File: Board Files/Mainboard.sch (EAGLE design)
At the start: 109 parts, among them J1 I2C Display

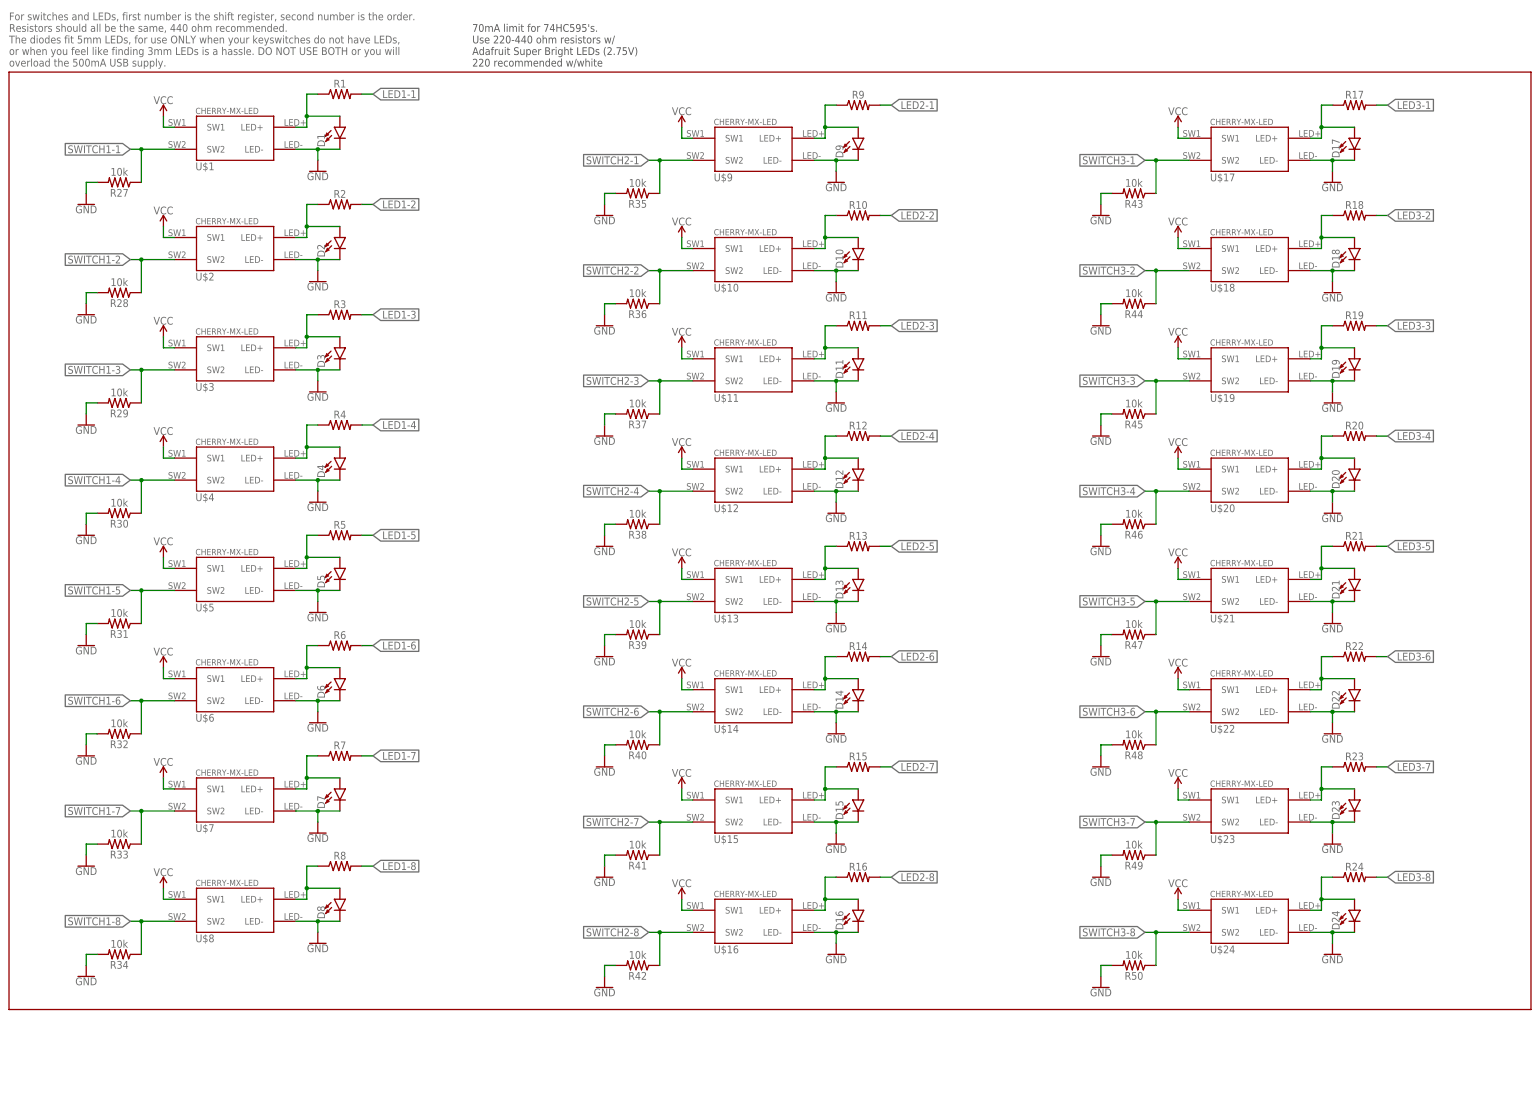
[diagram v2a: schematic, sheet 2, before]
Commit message: Completed First Schematic Draft
-Switched to Sparkfun Cherry parts
-Added illuminated rotary encoder
-Connected all microcontroller pins
-Finished shift register pins
-Added octave shift buttons
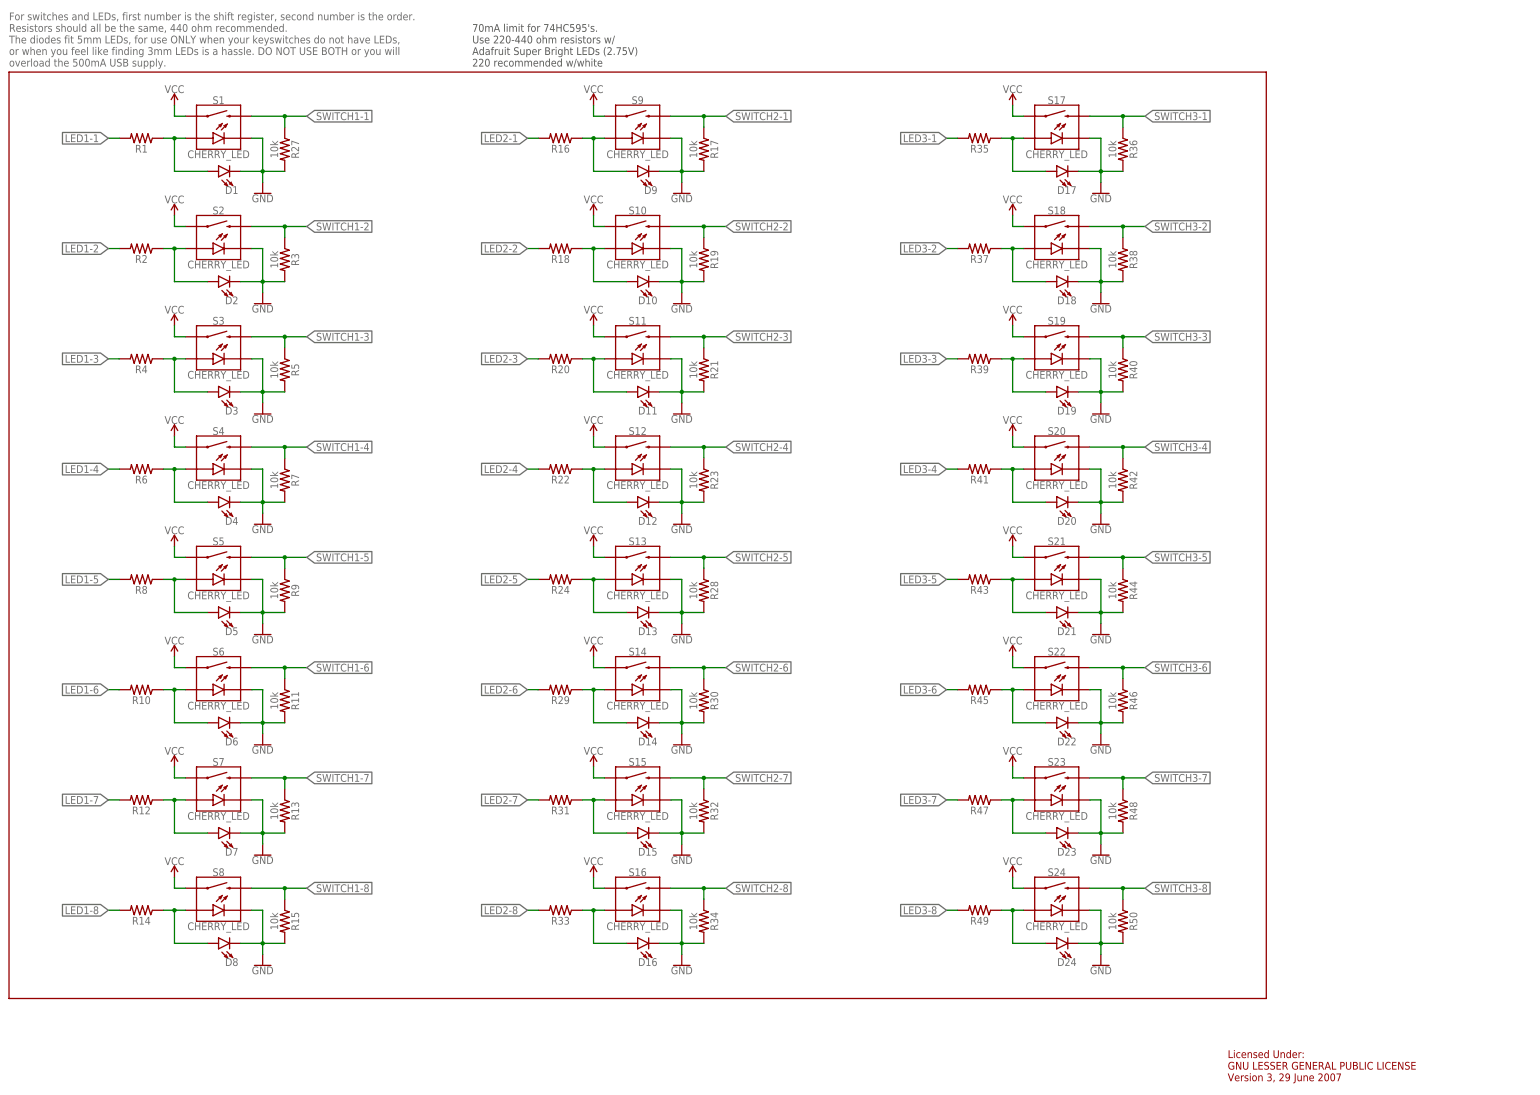
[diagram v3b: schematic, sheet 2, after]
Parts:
- removed U$1, U$10, U$11, U$12, U$13, U$14, U$15, U$16, U$17, U$18, U$19, U$2, U$20, U$21, U$22, U$23, U$24, U$3, U$4, U$5, U$6, U$7, U$8, U$9: CHERRY-MX-LED, cherrymx:CHERRY-MX-LED
- added R51, R52, R55: 10k, SparkFun-Resistors:10KOHM-HORIZ-1/4W-1%
- added S10, S11, S12, S13, S14, S15, S16, S17, S18, S19, S2, S20, S21, S22, S23, S24, S26, S27, S3, S4, S5, S6, S7, S8, S9: CHERRY_LED, SparkFun-Switches:MOMENTARY-SWITCH-SPST-LED-PTH-CHERRY
- added S25: 6MM_SPST_SMD_SWITCH, SparkFun-Switches:MOMENTARY-SWITCH-SPST-SMD-6.0X3.5MM
- added S28: ENCODER-2LED, SparkFun-Switches:ENCODER-2LED
- R11, R13, R15, R17, R19, R21, R23, R3, R5, R7, R9: value (none) -> 10k; device SparkFun-Resistors:RESISTORAXIAL-0.3 -> SparkFun-Resistors:10KOHM-HORIZ-1/4W-1%
- R29, R31, R33, R35, R37, R39, R41, R43, R45, R47, R49: value 10k -> (none); device SparkFun-Resistors:10KOHM-HORIZ-1/4W-1% -> SparkFun-Resistors:RESISTORAXIAL-0.3
- S1: value MOMENTARY-SWITCH-6MM-SMD -> CHERRY_LED; device SparkFun-Switches:MOMENTARY-SWITCH-SPST-SMD-6.0X3.5MM -> SparkFun-Switches:MOMENTARY-SWITCH-SPST-LED-PTH-CHERRY
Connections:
- removed net LED_CLOCK: B1.*5, LED_REG_1.SCK, LED_REG_2.SCK, LED_REG_3.SCK
- removed net N$28: B1.7
- removed net N$29: B1.8
- new net ENCODER_ANALOG: B1.A0, S28.B
- new net ENCODER_DIGITAL: B1.13(SCK), S28.A
- new net ENCODER_GREEN: B1.A2, S28.+G
- new net ENCODER_RED: B1.A1, S28.+R
- new net ENCODER_SWITCH: B1.A3, R55.1, S28.SW
- new net LED_OUTPUT_EN: B1.*6
- new net OCTAVE_DOWN: B1.11(MOSI), R52.2, S27.2
- new net OCTAVE_UP: B1.12(MISO), R51.2, S26.2
- new net REGISTER_CLOCK: B1.*9, KEY_REG_1A.CLK, LED_REG_1.SCK, LED_REG_2.SCK, LED_REG_3.SCK
- net GND: now also B1.GND@2, R11.2, R13.2, R15.2, R17.2, R19.2, R21.2, R23.2, R3.2, R5.2, R51.1, R52.1, R7.2, R9.2, S1.C, S10.C, S11.C, S12.C, S13.C, S14.C, S15.C, S16.C, S17.C, S18.C, S19.C, S2.C, S20.C, S21.C, S22.C, S23.C, S24.C, S25.2, S28.-, S28.C, S3.C, S4.C, S5.C, S6.C, S7.C, S8.C, S9.C; no longer R29.2, R31.2, R33.2, R35.2, R37.2, R39.2, R41.2, R43.2, R45.2, R47.2, R49.2, S1.2, U$1.LED-, U$10.LED-, U$11.LED-, U$12.LED-, U$13.LED-, U$14.LED-, U$15.LED-, U$16.LED-, U$17.LED-, U$18.LED-, U$19.LED-, U$2.LED-, U$20.LED-, U$21.LED-, U$22.LED-, U$23.LED-, U$24.LED-, U$3.LED-, U$4.LED-, U$5.LED-, U$6.LED-, U$7.LED-, U$8.LED-, U$9.LED-
- net KEY_CLOCK: no longer KEY_REG_1A.CLK
- net KEY_DATA: now also B1.7
- net KEY_LATCH: now also B1.8
- net LED1-3: now also R4.2; no longer R3.2
- net LED1-4: now also R6.2; no longer R4.2
- net LED1-5: now also R8.2; no longer R5.2
- net LED1-6: now also R10.2; no longer R6.2
- net LED1-7: now also R12.2; no longer R7.2
- net LED1-8: now also R14.2; no longer R8.2
- net LED2-1: now also R16.2; no longer R9.2
- net LED2-2: now also R18.2; no longer R10.2
- net LED2-3: now also R20.2; no longer R11.2
- net LED2-4: now also R22.2; no longer R12.2
- net LED2-5: now also R24.2; no longer R13.2
- net LED2-6: now also R29.2; no longer R14.2
- net LED2-7: now also R31.2; no longer R15.2
- net LED2-8: now also R33.2; no longer R16.2
- net LED3-1: now also R35.2; no longer R17.2
- net LED3-2: now also R37.2; no longer R18.2
- net LED3-3: now also R39.2; no longer R19.2
- net LED3-4: now also R41.2; no longer R20.2
- net LED3-5: now also R43.2; no longer R21.2
- net LED3-6: now also R45.2; no longer R22.2
- net LED3-7: now also R47.2; no longer R23.2
- net LED3-8: now also R49.2; no longer R24.2
- net LED_LATCH: now also B1.*5; no longer B1.*6
- net N$1: now also S1.A; no longer U$1.LED+
- net N$10: now also R18.1, S10.A; no longer R10.1, U$10.LED+
- net N$11: now also R20.1, S11.A; no longer R11.1, U$11.LED+
- net N$12: now also R22.1, S12.A; no longer R12.1, U$12.LED+
- net N$13: now also R24.1, S13.A; no longer R13.1, U$13.LED+
- net N$14: now also R29.1, S14.A; no longer R14.1, U$14.LED+
- net N$15: now also R31.1, S15.A; no longer R15.1, U$15.LED+
- net N$16: now also R33.1, S16.A; no longer R16.1, U$16.LED+
- net N$17: now also R35.1, S17.A; no longer R17.1, U$17.LED+
- net N$18: now also R37.1, S18.A; no longer R18.1, U$18.LED+
- net N$19: now also R39.1, S19.A; no longer R19.1, U$19.LED+
- net N$2: now also S2.A; no longer U$2.LED+
- net N$20: now also R41.1, S20.A; no longer R20.1, U$20.LED+
- net N$21: now also R43.1, S21.A; no longer R21.1, U$21.LED+
- net N$22: now also R45.1, S22.A; no longer R22.1, U$22.LED+
- net N$23: now also R47.1, S23.A; no longer R23.1, U$23.LED+
- net N$24: now also R49.1, S24.A; no longer R24.1, U$24.LED+
- net N$3: now also R4.1, S3.A; no longer R3.1, U$3.LED+
- net N$4: now also R6.1, S4.A; no longer R4.1, U$4.LED+
- net N$5: now also R8.1, S5.A; no longer R5.1, U$5.LED+
- net N$6: now also R10.1, S6.A; no longer R6.1, U$6.LED+
- net N$7: now also R12.1, S7.A; no longer R7.1, U$7.LED+
- net N$8: now also R14.1, S8.A; no longer R8.1, U$8.LED+
- net N$9: now also R16.1, S9.A; no longer R9.1, U$9.LED+
- net RESET: now also S25.1; no longer S1.1
- net SWITCH1-1: now also S1.2; no longer U$1.SW2
- net SWITCH1-2: now also R3.1, S2.2; no longer R28.1, U$2.SW2
- net SWITCH1-3: now also R5.1, S3.2; no longer R29.1, U$3.SW2
- net SWITCH1-4: now also R7.1, S4.2; no longer R30.1, U$4.SW2
- net SWITCH1-5: now also R9.1, S5.2; no longer R31.1, U$5.SW2
- net SWITCH1-6: now also R11.1, S6.2; no longer R32.1, U$6.SW2
- net SWITCH1-7: now also R13.1, S7.2; no longer R33.1, U$7.SW2
- net SWITCH1-8: now also R15.1, S8.2; no longer R34.1, U$8.SW2
- net SWITCH2-1: now also R17.1, S9.2; no longer R35.1, U$9.SW2
- net SWITCH2-2: now also R19.1, S10.2; no longer R36.1, U$10.SW2
- net SWITCH2-3: now also R21.1, S11.2; no longer R37.1, U$11.SW2
- net SWITCH2-4: now also R23.1, S12.2; no longer R38.1, U$12.SW2
- net SWITCH2-5: now also R28.1, S13.2; no longer R39.1, U$13.SW2
- net SWITCH2-6: now also R30.1, S14.2; no longer R40.1, U$14.SW2
- net SWITCH2-7: now also R32.1, S15.2; no longer R41.1, U$15.SW2
- net SWITCH2-8: now also R34.1, S16.2; no longer R42.1, U$16.SW2
- net SWITCH3-1: now also R36.1, S17.2; no longer R43.1, U$17.SW2
- net SWITCH3-2: now also R38.1, S18.2; no longer R44.1, U$18.SW2
- net SWITCH3-3: now also R40.1, S19.2; no longer R45.1, U$19.SW2
- net SWITCH3-4: now also R42.1, S20.2; no longer R46.1, U$20.SW2
- net SWITCH3-5: now also R44.1, S21.2; no longer R47.1, U$21.SW2
- net SWITCH3-6: now also R46.1, S22.2; no longer R48.1, U$22.SW2
- net SWITCH3-7: now also R48.1, S23.2; no longer R49.1, U$23.SW2
- net SWITCH3-8: now also S24.2; no longer U$24.SW2
- net VCC: now also B1.VCC, R55.2, S1.1, S10.1, S11.1, S12.1, S13.1, S14.1, S15.1, S16.1, S17.1, S18.1, S19.1, S2.1, S20.1, S21.1, S22.1, S23.1, S24.1, S26.1, S27.1, S3.1, S4.1, S5.1, S6.1, S7.1, S8.1, S9.1; no longer U$1.SW1, U$10.SW1, U$11.SW1, U$12.SW1, U$13.SW1, U$14.SW1, U$15.SW1, U$16.SW1, U$17.SW1, U$18.SW1, U$19.SW1, U$2.SW1, U$20.SW1, U$21.SW1, U$22.SW1, U$23.SW1, U$24.SW1, U$3.SW1, U$4.SW1, U$5.SW1, U$6.SW1, U$7.SW1, U$8.SW1, U$9.SW1
- net VELPOT: now also B1.*10; no longer B1.*9
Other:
- note added: "Encoder Menu Controller"
- note added: "Licensed Under: GNU LESSER GENERAL PUBLIC LICENSE Version 3, 29 June 2007"
- note added: "Octave Shift Buttons"
- note added: "Pro Micro"
- moved on the sheet: B1, C1, D1, D10, D11, D12, D13, D14, D15, D16, D17, D18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
